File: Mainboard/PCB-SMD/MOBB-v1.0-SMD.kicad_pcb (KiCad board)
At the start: 2 copper layers, 85.6 x 49.7 mm, 65 parts, among them P1 AUX 1-3, P14 EXTRA Pins, P2 Wire to Teensy VUSB, P3 +3.3V, P4 Pit Limiter, P5 Rotary Encoders, P6 BTN 1-32, Q1 NPN, Q2 NPN, Q3 NPN, Q4 NPN, U1 74HC4051, U2 74HC4051, U3 74HC4051, U4 74HC4051, U5 Teensy3.2

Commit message: * new layout (wip)
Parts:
- R11, R12, R13, R14, R15, R16, R19, R20, R22, R23, R25, R26, R28, R29, R30, R31, R32, R33, R34, R35, R36, R37, R38, R39, R4, R40, R41, R42, R43, R44, R5, R6, R7, R8, R9: moved to B.Cu
- moved R24 79.4 mm to (188.0, 142.3)
- moved R17 76.1 mm to (204.4, 128.5), turned to 90 degrees
- moved R18 66.0 mm to (211.4, 128.5), turned to 90 degrees
- moved R21 57.1 mm to (218.5, 131.3), turned to 90 degrees
- moved U4 43.1 mm to (251.2, 109.9), turned to 270 degrees
- moved P2 38.1 mm to (191.6, 121.1)
- moved Q1 37.9 mm to (201.5, 128.2), turned to 90 degrees
- moved Q2 37.9 mm to (208.5, 128.2), turned to 90 degrees
- moved Q3 34.0 mm to (215.6, 131.0), turned to 90 degrees
- moved PTC2 32.5 mm to (216.4, 122.2)
- moved R1 32.1 mm to (242.1, 124.1), turned to 180 degrees
- moved U3 31.1 mm to (220.6, 110.0), turned to 270 degrees
- moved PTC1 30.5 mm to (196.1, 123.2), turned to 90 degrees
- moved R6 29.2 mm to (200.7, 127.9), turned to 270 degrees
- moved R2 28.2 mm to (182.8, 120.0), turned to 180 degrees
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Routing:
- net +3V3: track 0.00 -> 117.3 mm, vias 0 -> 7
- net PINHEADERSRC: track 0.00 -> 104.8 mm
- net Net-(U2-Pad3): track 0.00 -> 73.1 mm
- net Net-(U1-Pad3): track 0.00 -> 57.1 mm
- net Net-(P6-Pad47): track 0.00 -> 34.3 mm
- net Net-(P6-Pad45): track 0.00 -> 32.8 mm
- net Net-(P6-Pad51): track 0.00 -> 30.5 mm, vias 0 -> 2
- net Net-(P6-Pad53): track 0.00 -> 30.1 mm, vias 0 -> 2
- net GND: track 0.00 -> 26.2 mm, vias 0 -> 6
- net Net-(U4-Pad3): track 0.00 -> 24.8 mm, vias 0 -> 2
- net Net-(U3-Pad3): track 0.00 -> 24.4 mm, vias 0 -> 2
- net Net-(P6-Pad61): track 0.00 -> 23.9 mm, vias 0 -> 1
- net Net-(P6-Pad31): track 20.9 -> 41.9 mm
- net Net-(P6-Pad59): track 0.00 -> 20.3 mm, vias 0 -> 1
- net Net-(P6-Pad49): track 0.00 -> 18.6 mm
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
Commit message: * bit messy but the layout should work. still WIP
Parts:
- added P7: LED, Socket_Strips:Socket_Strip_Straight_1x02, F.Cu at (208.0, 110.8)
- R3: moved to B.Cu
- moved C4 41.9 mm to (201.7, 120.6), turned to 0 degrees
- moved R1 31.1 mm to (212.4, 114.8)
- moved R24 9.15 mm to (190.5, 133.5), turned to 90 degrees
- moved R27 7.40 mm to (196.3, 133.5), turned to 270 degrees
- moved Q4 4.61 mm to (193.4, 133.2)
- moved R10 4.00 mm to (186.6, 133.0)
- moved R3 3.79 mm to (192.6, 132.9)
- moved Q2 2.79 mm to (208.6, 131.0)
- moved R18 2.79 mm to (211.5, 131.3)
- moved R5 2.79 mm to (207.8, 130.7)
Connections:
- U5 pad 21: /reserved_for_4051 -> (no net)
- U5 pad 27: Net-(U5-Pad27) -> (no net)
- U5 pad 28: Net-(U5-Pad28) -> (no net)
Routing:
- net Net-(R24-Pad2): track 0.00 -> 57.6 mm, vias 0 -> 2
- net Net-(R17-Pad2): track 0.00 -> 41.7 mm
- net +3V3: track 117.3 -> 154.9 mm, vias 7 -> 8
- net Net-(R18-Pad2): track 0.00 -> 32.2 mm
- net Net-(U1-Pad11): track 0.00 -> 31.0 mm, vias 0 -> 1
- net Net-(P14-Pad2): track 0.00 -> 29.7 mm
- net Net-(U1-Pad10): track 0.00 -> 28.6 mm, vias 0 -> 1
- net Net-(P14-Pad1): track 0.00 -> 27.3 mm
- net Net-(U1-Pad9): track 0.00 -> 26.3 mm, vias 0 -> 1
- net +5V: track 10.2 -> 31.3 mm
- net Net-(P5-Pad6): track 0.00 -> 19.1 mm
- net Net-(P5-Pad3): track 0.00 -> 19.1 mm
- net Net-(P5-Pad2): track 0.00 -> 18.8 mm
- net Net-(P5-Pad5): track 0.00 -> 18.4 mm
- net Net-(P5-Pad1): track 0.00 -> 18.1 mm
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
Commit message: * tweaked
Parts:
- C4: footprint Capacitors_ThroughHole:C_Disc_D3.0mm_W2.0mm_P2.50mm -> Capacitors_SMD:C_0805_HandSoldering
- P1, P3: footprint Pin_Headers:Pin_Header_Angled_2x03 -> Pin_Headers:Pin_Header_Angled_2x03_Pitch2.54mm
- P14: footprint Pin_Headers:Pin_Header_Angled_1x05 -> Pin_Headers:Pin_Header_Angled_1x05_Pitch2.54mm
- P2: value Wire to Teensy VUSB -> VUSB; footprint Socket_Strips:Socket_Strip_Straight_1x01 -> Pin_Headers:Pin_Header_Straight_1x01_Pitch2.54mm
- P4: footprint Pin_Headers:Pin_Header_Angled_1x02 -> Pin_Headers:Pin_Header_Angled_1x02_Pitch2.54mm
- P5: footprint Pin_Headers:Pin_Header_Angled_1x06 -> Pin_Headers:Pin_Header_Angled_1x06_Pitch2.54mm
- P6: footprint Pin_Headers:Pin_Header_Angled_2x32 -> Pin_Headers:Pin_Header_Angled_2x32_Pitch2.54mm
- P7: footprint Socket_Strips:Socket_Strip_Straight_1x02 -> Pin_Headers:Pin_Header_Angled_1x02_Pitch2.54mm
- moved C1 56.0 mm to (236.8, 110.1), turned to 180 degrees
- moved R1 32.5 mm to (191.1, 139.4), turned to 270 degrees
- moved P7 32.0 mm to (196.6, 140.7), turned to 270 degrees
- moved C4 14.2 mm to (211.3, 110.1), turned to 180 degrees
- moved PTC2 10.3 mm to (209.9, 114.2)
- moved P2 1.98 mm to (190.0, 122.2)
- moved R10 1.84 mm to (188.4, 133.5)
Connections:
- U5 pad 21: (no net) -> /reserved_for_4051
- U5 pad 27: (no net) -> Net-(U5-Pad27)
- U5 pad 28: (no net) -> Net-(U5-Pad28)
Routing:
- net Net-(R1-Pad1): track 0.00 -> 99.7 mm, vias 0 -> 3
- net +3V3: track 154.9 -> 194.2 mm, vias 8 -> 10
- net Net-(P14-Pad4): track 0.00 -> 36.5 mm
- net Net-(P14-Pad5): track 0.00 -> 36.1 mm
- net Net-(P14-Pad3): track 0.00 -> 32.4 mm
- net Net-(U1-Pad11): track 31.0 -> 48.8 mm, vias 1 -> 3
- net Net-(U1-Pad9): track 26.3 -> 43.7 mm, vias 1 -> 3
- net Net-(U1-Pad10): track 28.6 -> 45.9 mm, vias 1 -> 3
- net GND: track 27.8 -> 37.8 mm, vias 7 -> 10
- net Net-(PTC2-Pad2): track 12.0 -> 18.7 mm
- net Net-(P7-Pad2): track 0.00 -> 3.00 mm
- net Net-(Q4-Pad1): track 2.01 -> 4.15 mm
- net Net-(P2-Pad1): track 4.67 -> 6.76 mm
- net Net-(P14-Pad2): track 29.7 -> 30.5 mm

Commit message: * RC1 for SMD PCB, still WIP
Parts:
- moved P2 10.5 mm to (200.4, 121.7)
- moved R2 6.39 mm to (189.2, 119.5)
- moved C7 6.31 mm to (189.1, 121.8)
- moved R1 1.05 mm to (190.5, 138.5)
- moved PTC1 1.01 mm to (195.8, 124.2)
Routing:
- net PINHEADERSRC: track 104.8 -> 270.0 mm
- net Net-(U1-Pad11): track 48.8 -> 103.1 mm, vias 3 -> 9
- net Net-(U1-Pad10): track 45.9 -> 99.7 mm, vias 3 -> 9
- net Net-(U1-Pad9): track 43.7 -> 95.4 mm, vias 3 -> 9
- net +3V3: track 194.2 -> 219.9 mm, vias 10 -> 11
- net Net-(R1-Pad1): track 99.7 -> 89.9 mm
- net Net-(P6-Pad45): track 32.8 -> 27.0 mm
- net Net-(P6-Pad47): track 34.3 -> 37.8 mm
- net Net-(P2-Pad1): track 6.76 -> 9.27 mm
- net Net-(U1-Pad3): track 57.1 -> 55.5 mm
- net Net-(U2-Pad3): track 73.1 -> 71.6 mm
- net Net-(P4-Pad2): track 9.24 -> 8.09 mm
- net +5V: track 31.3 -> 30.2 mm
- net Net-(P7-Pad2): track 3.00 -> 3.93 mm
- net Net-(R24-Pad2): track 57.6 -> 56.9 mm
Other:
- board text added: "LED"
- board text added: "Modular Open Button Box (MOBB) PCB rev RC1-SMD"
- board text removed: "11mm"
- board text removed: "5mm"
- board text removed: "Modular Open Button Box (MOBB) PCB rev 1.0"

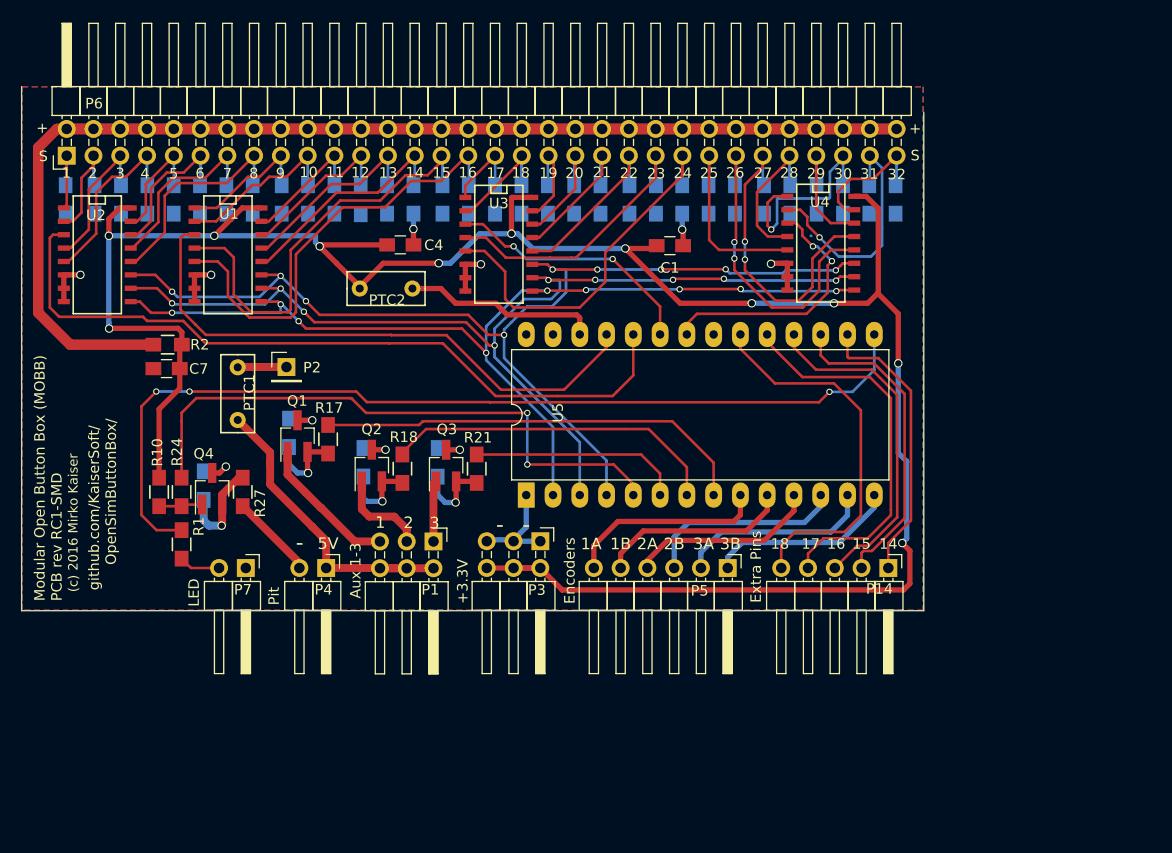
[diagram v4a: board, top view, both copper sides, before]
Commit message: * added top mounting hole to SMD PCB
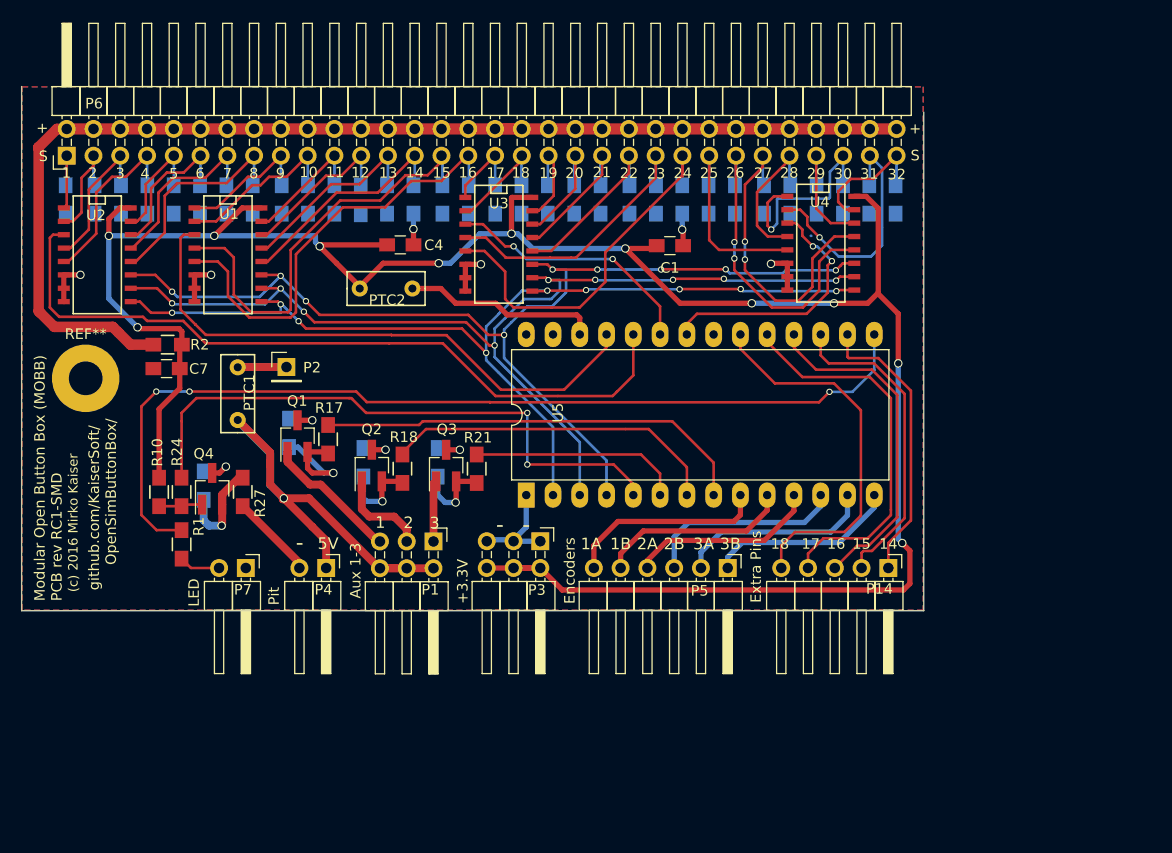
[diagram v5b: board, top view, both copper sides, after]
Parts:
- added REF**: MountingHole_3.2mm_M3_Pad, Mounting_Holes:MountingHole_3.2mm_M3_Pad, F.Cu at (181.4, 122.7)
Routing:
- net +5V: track 30.2 -> 46.5 mm, vias 0 -> 1
- net Net-(Q1-Pad2): track 7.81 -> 11.4 mm
- net +3V3: track 219.9 -> 217.9 mm
- net Net-(P1-Pad5): track 14.1 -> 12.6 mm

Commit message: * added bottom mounting hole and ground connections
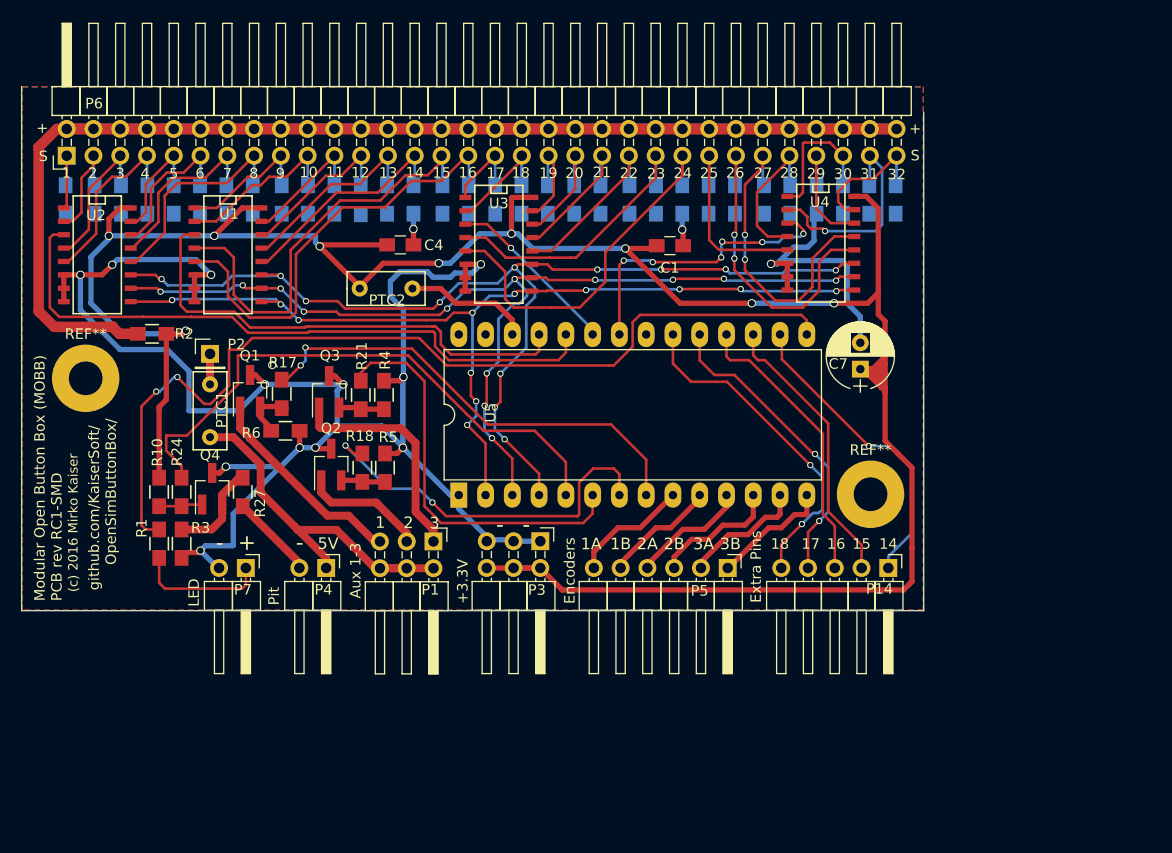
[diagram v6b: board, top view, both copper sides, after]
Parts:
- added REF**: MountingHole_3.2mm_M3_Pad, Mounting_Holes:MountingHole_3.2mm_M3_Pad, F.Cu at (255.9, 133.7)
- C7: footprint Capacitors_SMD:C_0805_HandSoldering -> Capacitors_ThroughHole:CP_Radial_D6.3mm_P2.50mm
- R3, R4, R5, R6: moved to F.Cu
- moved C7 65.8 mm to (254.9, 121.8), turned to 90 degrees
- moved Q3 13.1 mm to (204.5, 124.0)
- moved R21 13.0 mm to (207.5, 124.3)
- moved R4 8.18 mm to (209.7, 124.3)
- moved P2 7.36 mm to (193.2, 120.4)
- moved U5 6.40 mm to (216.8, 133.8)
- moved Q1 6.22 mm to (197.0, 123.9)
- moved R17 6.15 mm to (200.0, 124.2)
- moved R3 5.90 mm to (190.5, 138.4), turned to 90 degrees
- moved Q2 3.85 mm to (204.7, 130.9)
- moved R18 3.80 mm to (207.7, 131.2)
- moved PTC1 3.09 mm to (193.2, 125.8)
- moved R1 2.13 mm to (188.4, 138.4)
- moved R5 2.11 mm to (209.8, 131.2)
- moved R2 1.80 mm to (187.7, 118.5)
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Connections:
- P7 pad 1: GND -> Net-(P7-Pad1)
- P7 pad 2: Net-(P7-Pad2) -> GND
- R1 pad 2: Net-(P7-Pad2) -> Net-(P7-Pad1)
- U5 pad 21: /reserved_for_4051 -> (no net)
- U5 pad 27: Net-(U5-Pad27) -> (no net)
- U5 pad 28: Net-(U5-Pad28) -> (no net)
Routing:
- net GND: track 37.8 -> 191.8 mm, vias 10 -> 15
- net +3V3: track 217.9 -> 239.2 mm, vias 11 -> 9
- net Net-(R21-Pad2): track 20.2 -> 38.6 mm
- net Net-(P1-Pad1): track 6.16 -> 22.0 mm
- net Net-(P7-Pad1): track 0.00 -> 12.6 mm
- net +5V: track 46.5 -> 35.4 mm, vias 1 -> 0
- net Net-(U2-Pad3): track 71.6 -> 62.0 mm
- net Net-(U1-Pad3): track 55.5 -> 46.4 mm
- net Net-(P5-Pad6): track 19.1 -> 11.3 mm
- net Net-(U3-Pad3): track 24.4 -> 16.7 mm, vias 2 -> 1
- net Net-(P5-Pad5): track 18.4 -> 10.8 mm
- net Net-(P14-Pad4): track 36.5 -> 29.2 mm, vias 0 -> 2
- net Net-(P1-Pad5): track 12.6 -> 19.8 mm
- net Net-(P5-Pad2): track 18.8 -> 11.8 mm
- net Net-(P5-Pad3): track 19.1 -> 12.2 mm
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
